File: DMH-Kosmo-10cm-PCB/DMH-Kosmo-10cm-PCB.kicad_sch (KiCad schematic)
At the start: 0 parts

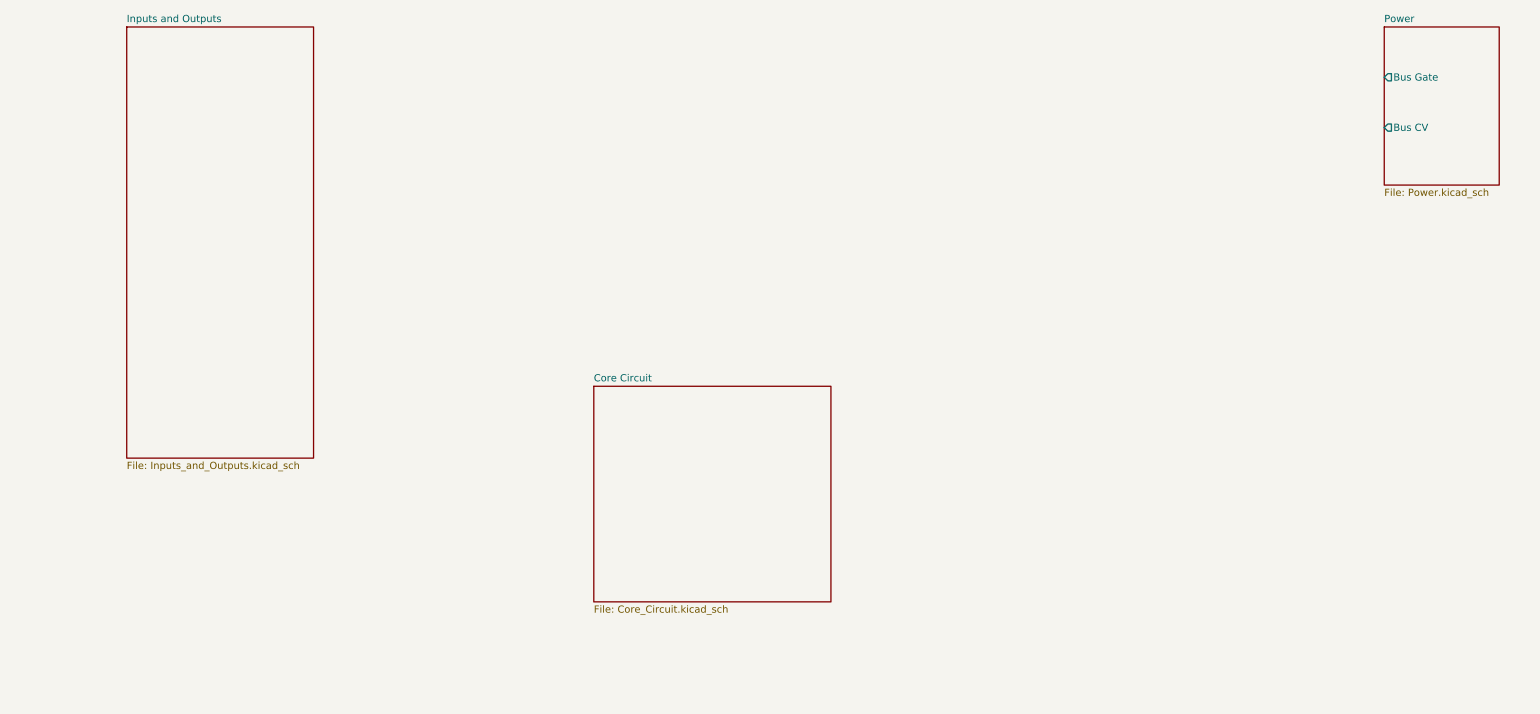
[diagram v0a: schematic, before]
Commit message: Created 10cm PCB layout template
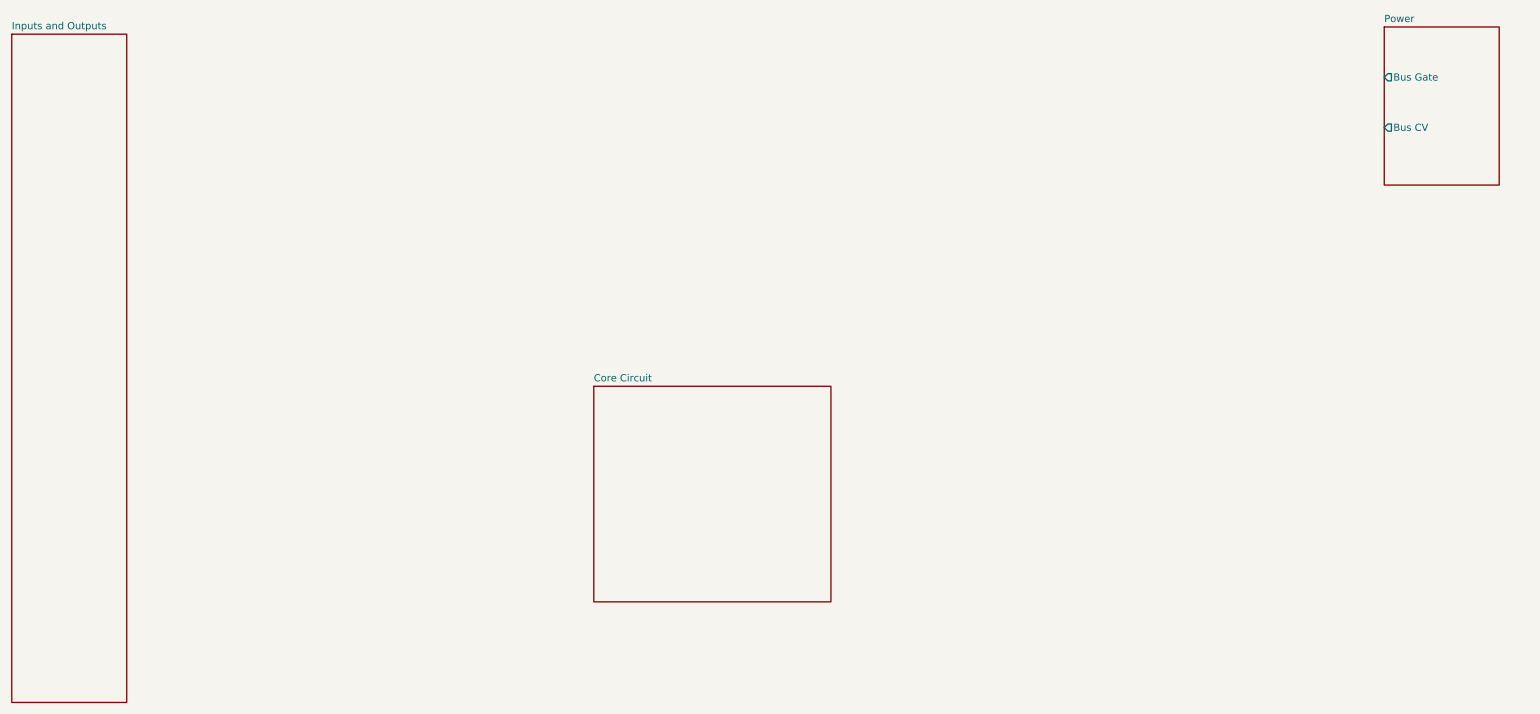
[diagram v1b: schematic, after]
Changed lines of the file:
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@@
 				)
 				(justify left top)
+				(hide yes)
 			)
 		)
@@
 				)
 				(justify left top)
+				(hide yes)
 			)
 		)
@@
 	)
 	(sheet
-		(at 38.1 16.51)
-		(size 33.02 76.2)
+		(at 17.78 17.78)
+		(size 20.32 118.11)
 		(fields_autoplaced yes)
 		(stroke
@@
 		)
 		(property "Sheetname" "Inputs and Outputs"
-			(at 38.1 15.7984 0)
+			(at 17.78 17.0684 0)
 			(effects
 				(font
@@
 		)
 		(property "Sheetfile" "Inputs_and_Outputs.kicad_sch"
-			(at 38.1 93.2946 0)
+			(at 17.78 136.4746 0)
 			(effects
 				(font
@@
 				)
 				(justify left top)
+				(hide yes)
 			)
 		)

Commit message: Minor fixes on schematic templates
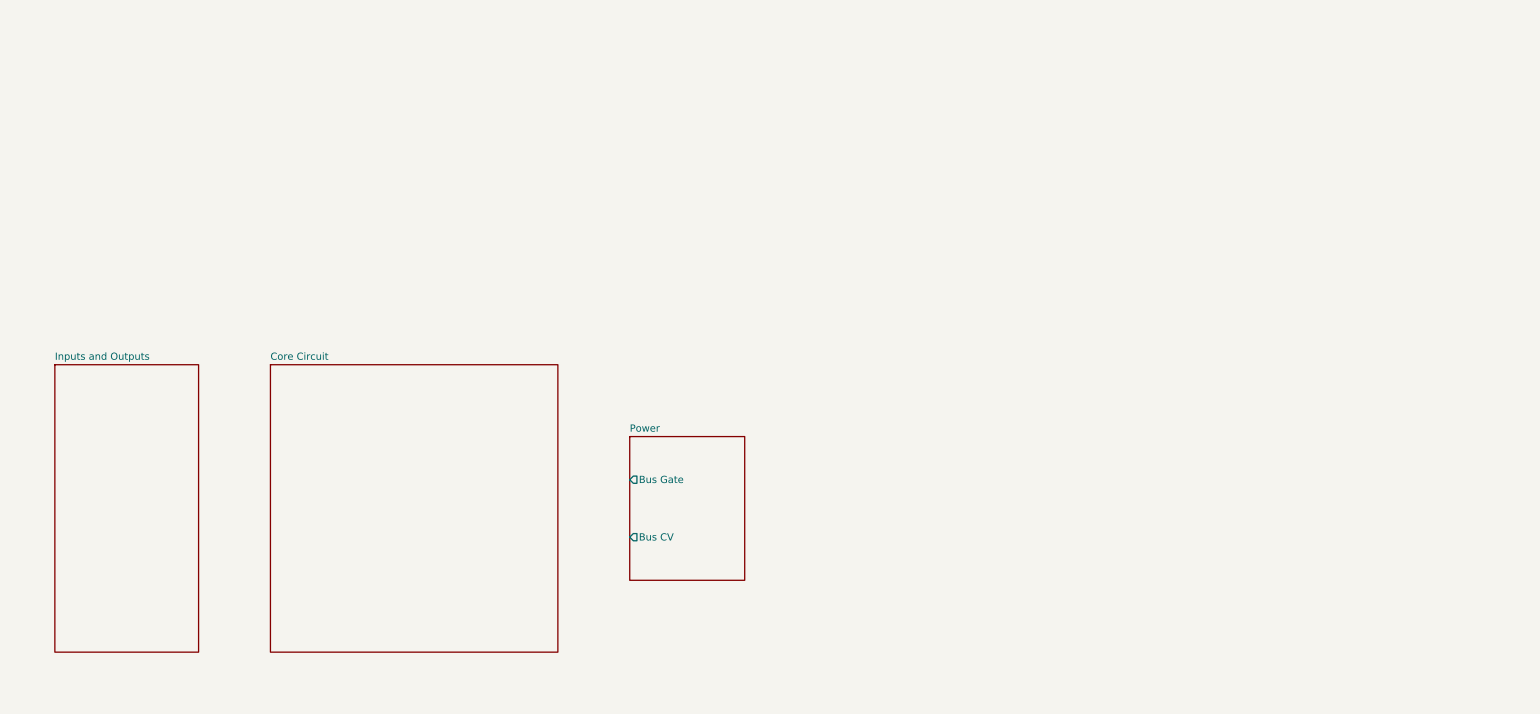
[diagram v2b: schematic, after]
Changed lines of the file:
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@@
 	)
 	(sheet
-		(at 260.35 16.51)
-		(size 20.32 27.94)
+		(at 127 88.9)
+		(size 20.32 25.4)
 		(fields_autoplaced yes)
 		(stroke
@@
 		)
 		(property "Sheetname" "Power"
-			(at 260.35 15.7984 0)
+			(at 127 88.1884 0)
 			(effects
 				(font
@@
 		)
 		(property "Sheetfile" "Power.kicad_sch"
-			(at 260.35 45.0346 0)
+			(at 127 114.8846 0)
 			(effects
 				(font
@@
 		)
 		(pin "Bus Gate" output
-			(at 260.35 25.4 180)
+			(at 127 96.52 180)
 			(effects
 				(font
@@
 		)
 		(pin "Bus CV" output
-			(at 260.35 34.29 180)
+			(at 127 106.68 180)
 			(effects
 				(font
@@
 	)
 	(sheet
-		(at 120.65 80.01)
-		(size 41.91 38.1)
+		(at 63.5 76.2)
+		(size 50.8 50.8)
 		(fields_autoplaced yes)
 		(stroke
@@
 		)
 		(property "Sheetname" "Core Circuit"
-			(at 120.65 79.2984 0)
+			(at 63.5 75.4884 0)
 			(effects
 				(font
@@
 		)
 		(property "Sheetfile" "Core_Circuit.kicad_sch"
-			(at 120.65 118.6946 0)
+			(at 63.5 127.5846 0)
 			(effects
 				(font
@@
 	)
 	(sheet
-		(at 17.78 17.78)
-		(size 20.32 118.11)
+		(at 25.4 76.2)
+		(size 25.4 50.8)
 		(fields_autoplaced yes)
 		(stroke
@@
 		)
 		(property "Sheetname" "Inputs and Outputs"
-			(at 17.78 17.0684 0)
+			(at 25.4 75.4884 0)
 			(effects
 				(font
@@
 		)
 		(property "Sheetfile" "Inputs_and_Outputs.kicad_sch"
-			(at 17.78 136.4746 0)
+			(at 25.4 127.5846 0)
 			(effects
 				(font
